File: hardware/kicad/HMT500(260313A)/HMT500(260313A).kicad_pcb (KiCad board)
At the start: 4 copper layers, 56.5 x 23 mm, 84 parts, among them J1 SM08B-GHS-TB, J2 TC2030-IDC-NL, J3 SM04B-SRSS-TB, J5 CHASSIS wire, U1 TPS26600PWPR, U10 TPS26611DDFR, U11 THVD2450DR, U12 OPA197IDBVR, U13 OPA197IDBVR, U14 SN74LVC2G32DCUR, U2 LMR36006BRNXR, U3 TPS7A2033PDBVR, U4 STM32G0B1CCT3, U5 PCAP04-AQFM-24, U6 ADS1220IPWR, U7 DAC8760IPWP, U8 DAC8760IPWP, U9 TPS26611DDFR

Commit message: Mech Rev H: outline equal to E+E EE364 per section, assembly procedure HMT500-A-001
- Exposed probe 12 x 34 (cap +5.5, 25 holes), G1/2 14, hex AF27 x 10, body dia 30,
  seal face to end cap 77, M12 15, overall 140
- Housing 30/25 with M26x1 R/LH turnbuckle, O-ring 24 x 1.5 in dia 27, end cap flange 4 mm AF27,
  M16x1.5 at x 71-77 (connector thread <= 6 mm); internals shifted -2, PCB placement unchanged
- place_pcb: plan coordinates relative to PCB front (DX), bores from params
- Assembly sim 23 checks NG 0; drawings, STEP, renders, JLCCNC package, docs, decision #30
- New assembly_procedure.py: 19-step procedure PDF with 3D step illustrations

Co-Authored-By: Claude Opus 5.5 <noreply@anthropic.com>
Claude-Session: https://claude.ai/code/session_01JA2o8uJsqp9Vzsg4b665ev
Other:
- board text added: "11.5-48.9 mm: width 23, bore 25 -> edge 3.6 / center 11.2 mm"
- board text removed: "11.5-48.9 mm: width 23, bore 27 -> edge 5.8 / center 12.2 mm"

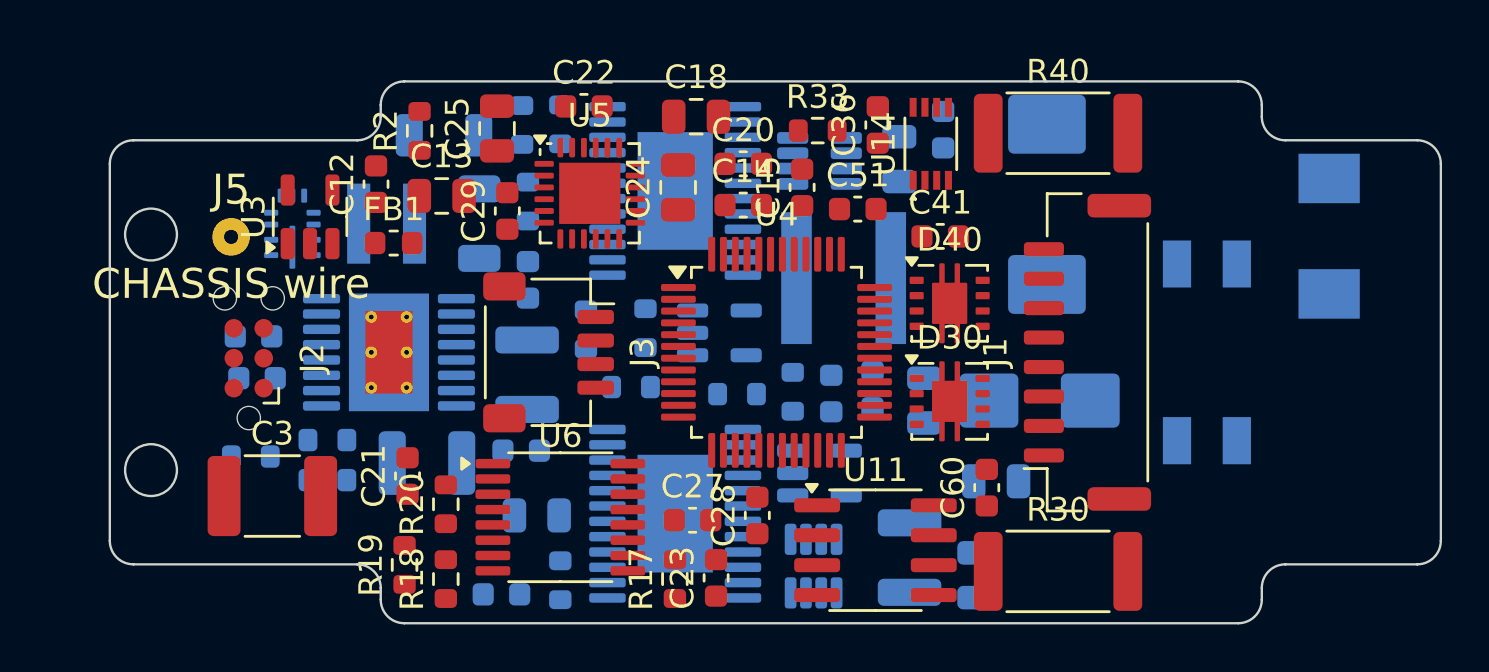
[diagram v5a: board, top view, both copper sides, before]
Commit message: Schematic v0.9 + placement rev 4: apply triple-review A/B items, re-review fixes
- Power: OVP 32.6 V (R5 36.5k), D2 TVS3301, C2 2.2u 100V, buck input 220n x2,
  U2 pin 3 = SW; TPS26611 +Vs emitter-follower clamp (Q1 MMBTA06, R50, D50 27V)
- RS-485: THVD2410, DE 10k pull-down (R60) for in-house bootloader
- MCU: SGOOD on PA0/PA4, CS_CDC PA15, VIN_SENSE PB0, LATCH/CS pull-ups,
  SWD no-connect removed, netlist checker flags no-connect on used pins
- Analog: OPA197 V+ = DAC AVDD, R31/R41 100k, local caps; X7R throughout
- New aux sheet; SOT-23 and R1206 footprints; parts list and JLC files
- Placement: pin-targeted hints, MCU decaps under U4, chassis parts grouped
  in front, J5 keep-out 3.3 mm, CHASSIS netclass; 102/102 parts placed
- Docs: final review H table, decision #32, circuit design, placement rev 4

Co-Authored-By: Claude Opus 5.5 <noreply@anthropic.com>
Claude-Session: https://claude.ai/code/session_01JA2o8uJsqp9Vzsg4b665ev
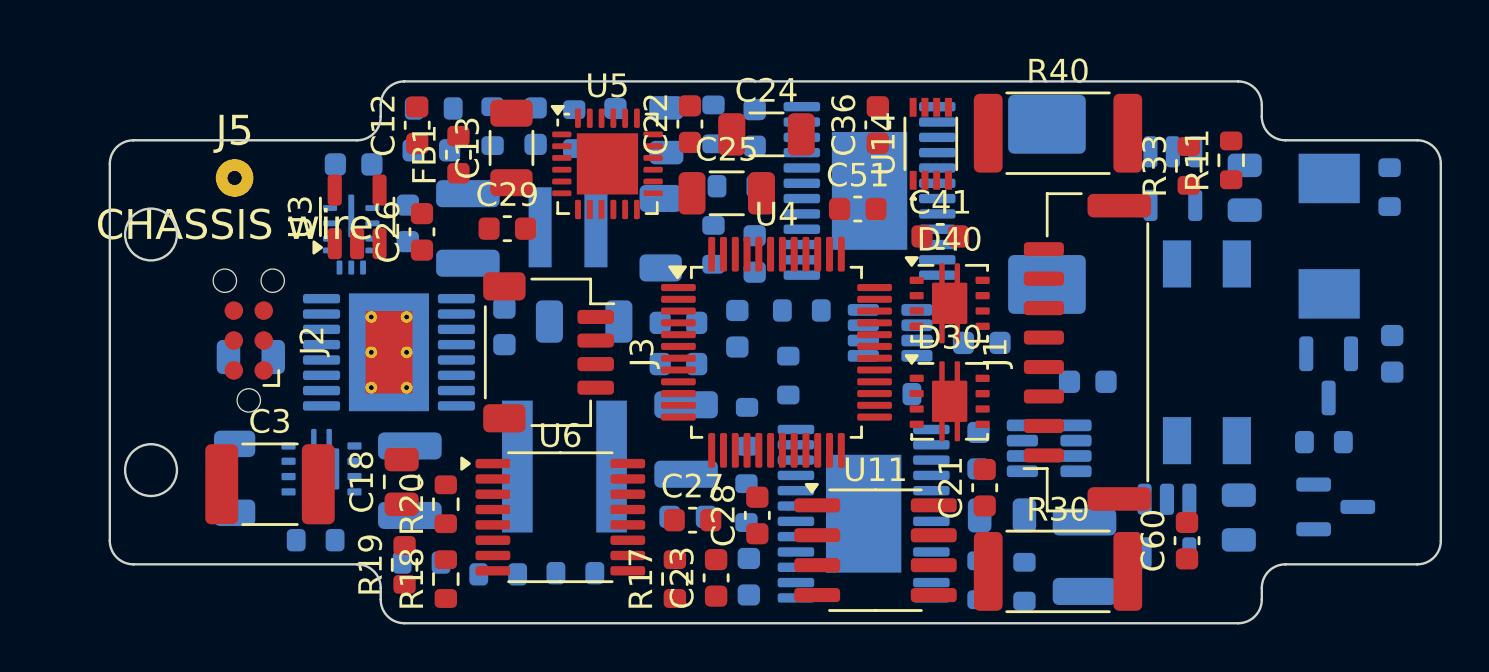
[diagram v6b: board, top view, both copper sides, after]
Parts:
- added C16: 220n 100V, Capacitor_SMD:C_0603_1608Metric, B.Cu at (110.3, 92.0)
- added C17: 220n 100V, Capacitor_SMD:C_0603_1608Metric, B.Cu at (112.7, 94.5)
- added C2: 2.2u 100V, Capacitor_SMD:C_1210_3225Metric, B.Cu at (112.7, 105.5)
- added C26: 1u, Capacitor_SMD:C_0603_1608Metric, F.Cu at (113.2, 94.9)
- added C30: 100n, Capacitor_SMD:C_0603_1608Metric, B.Cu at (124.5, 107.0)
- added C46: 100n, Capacitor_SMD:C_0603_1608Metric, B.Cu at (141.5, 101.2)
- added C53: 100n, Capacitor_SMD:C_0603_1608Metric, B.Cu at (154.4, 100.1)
- added C56: 100n, Capacitor_SMD:C_0603_1608Metric, B.Cu at (137.0, 99.6)
- added D50: BZX84C27, Package_TO_SOT_SMD:SOT-23, B.Cu at (152.0, 106.6)
- added Q1: MMBTA06, Package_TO_SOT_SMD:SOT-23, B.Cu at (151.7, 101.0)
- added R10: 10k, Resistor_SMD:R_0603_1608Metric, B.Cu at (126.6, 93.0)
- added R11: 10k, Resistor_SMD:R_0603_1608Metric, F.Cu at (147.6, 91.8)
- added R12: 100k, Resistor_SMD:R_0603_1608Metric, B.Cu at (119.8, 109.4)
- added R13: 100k, Resistor_SMD:R_0603_1608Metric, B.Cu at (125.6, 95.4)
- added R14: 100k 1%, Resistor_SMD:R_0603_1608Metric, B.Cu at (127.0, 103.2)
- added R15: 10k 1%, Resistor_SMD:R_0603_1608Metric, B.Cu at (128.8, 101.0)
- added R50: 10k, Resistor_SMD:R_0603_1608Metric, B.Cu at (151.5, 103.8)
- added R60: 10k, Resistor_SMD:R_0603_1608Metric, B.Cu at (127.0, 106.4)
- C13: footprint Capacitor_SMD:C_0805_2012Metric -> Capacitor_SMD:C_1206_3216Metric
- C14, C15, C20: moved to B.Cu
- C24: value 10u -> 22u 10V; footprint Capacitor_SMD:C_0805_2012Metric -> Capacitor_SMD:C_1206_3216Metric
- C25: value 4.7u -> 10u; footprint Capacitor_SMD:C_0805_2012Metric -> Capacitor_SMD:C_1206_3216Metric
- C27: value 10n -> 10n C0G
- D2: value SMBJ33CA -> TVS3301DRBR; footprint Diode_SMD:D_SMB -> HMT500_260313A:Texas_DRB0008A_PadFloat
- R2: value 1M -> 1M HV; footprint Resistor_SMD:R_0603_1608Metric -> Resistor_SMD:R_1206_3216Metric; moved to B.Cu
- R31, R41: value 10k -> 100k
- R5: value 41.2k 1% -> 36.5k 1%
- U11: value THVD2450DR -> THVD2410DR
- moved R41 32.2 mm to (154.3, 93.0)
- moved D2 30.6 mm to (109.0, 105.0)
- moved C1 28.6 mm to (106.0, 100.2), turned to 0 degrees
- moved C21 24.5 mm to (137.1, 105.8)
- moved C52 20.4 mm to (123.6, 90.6), turned to -90 degrees
- moved U13 20.3 mm to (145.1, 92.6), turned to -90 degrees
- moved C18 19.9 mm to (112.4, 105.5), turned to 90 degrees
- moved C42 19.8 mm to (137.9, 106.9)
- moved R34 17.8 mm to (136.9, 109.7)
- moved R2 16.7 mm to (105.3, 105.3), turned to -90 degrees
- moved R33 15.8 mm to (145.8, 92.1), turned to 90 degrees
- moved U12 14.9 mm to (144.9, 107.4), turned to -90 degrees
- moved C55 14.7 mm to (148.2, 93.0)
- moved C4 14.3 mm to (121.5, 90.4), turned to -90 degrees
- moved GDT1 14.3 mm to (119.3, 104.8)
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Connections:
- C45 pad 1: VIN_P -> DAC1_AVDD
- C55 pad 1: VIN_P -> DAC2_AVDD
- D2 pad 2: GND -> VIN_F
- U10 pad 6: VIN_P -> VS_CLAMP
- U12 pad 5: VIN_P -> DAC1_AVDD
- U13 pad 5: VIN_P -> DAC2_AVDD
- U2 pad 3: (no net) -> BUCK_SW
- U4 pad 11: (no net) -> OUT1_SGOOD
- U4 pad 15: (no net) -> OUT2_SGOOD
- U4 pad 19: CS_CDC -> VIN_SENSE
- U4 pad 30: OUT1_SGOOD -> (no net)
- U4 pad 31: OUT2_SGOOD -> (no net)
- U4 pad 37: (no net) -> CS_CDC
- U9 pad 6: VIN_P -> VS_CLAMP

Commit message: Map BOM to JLCPCB/LCSC parts (decision #34) and re-place
- 50 of 55 BOM lines have LCSC numbers (make_parts_list.LCSC); parts list
  gets LCSC / JLC class columns; JLC BOM and harness order filled
- Keep MCU (125 C grade), LMR36006, R19 precision ref and pulse resistors
  via JLC global sourcing
- LCSC-driven footprint changes: C6/C10 1210, C16/C17 0805, R1 2512,
  L2 XAL4040; C3 2 kV X7R 1812, GDT 2035-25, L1 SRF0905 (to verify)
- Re-placed: 102/102, netlist 77/77, assembly sim 23 OK

Co-Authored-By: Claude Opus 5.5 <noreply@anthropic.com>
Claude-Session: https://claude.ai/code/session_01JA2o8uJsqp9Vzsg4b665ev
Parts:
- C10, C6: footprint Capacitor_SMD:C_1206_3216Metric -> Capacitor_SMD:C_1210_3225Metric
- C16, C17: footprint Capacitor_SMD:C_0603_1608Metric -> Capacitor_SMD:C_0805_2012Metric
- C22: value 220p C0G 1% -> 330p C0G 1%
- C3: value 4.7n 2kV Y2 -> 4.7n 2kV
- L2: footprint Inductor_SMD:L_Coilcraft_XAL4030-XXX -> Inductor_SMD:L_Coilcraft_XAL4040-XXX
- R1: footprint Resistor_SMD:R_MELF_MMB-0207 -> Resistor_SMD:R_2512_6332Metric
- moved C11 13.7 mm to (123.5, 103.0)
- moved C4 13.1 mm to (125.2, 102.9)
- moved R8 9.49 mm to (116.8, 98.7), turned to -90 degrees
- moved C9 9.37 mm to (110.2, 92.2), turned to 0 degrees
- moved R15 9.26 mm to (138.1, 101.5), turned to 0 degrees
- moved C6 8.00 mm to (120.1, 90.7)
- moved R6 7.79 mm to (125.0, 96.3)
- moved R13 6.32 mm to (127.6, 101.4), turned to 0 degrees
- moved C10 5.35 mm to (120.1, 99.2), turned to 0 degrees
- moved C16 4.10 mm to (112.8, 95.3), turned to -90 degrees
- moved R14 3.75 mm to (130.1, 100.9)
- moved C30 3.25 mm to (124.5, 110.2)
- moved C7 3.25 mm to (124.5, 107.0)
- moved C17 2.46 mm to (113.7, 92.3), turned to 0 degrees
- moved L2 2.02 mm to (121.5, 94.9)
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
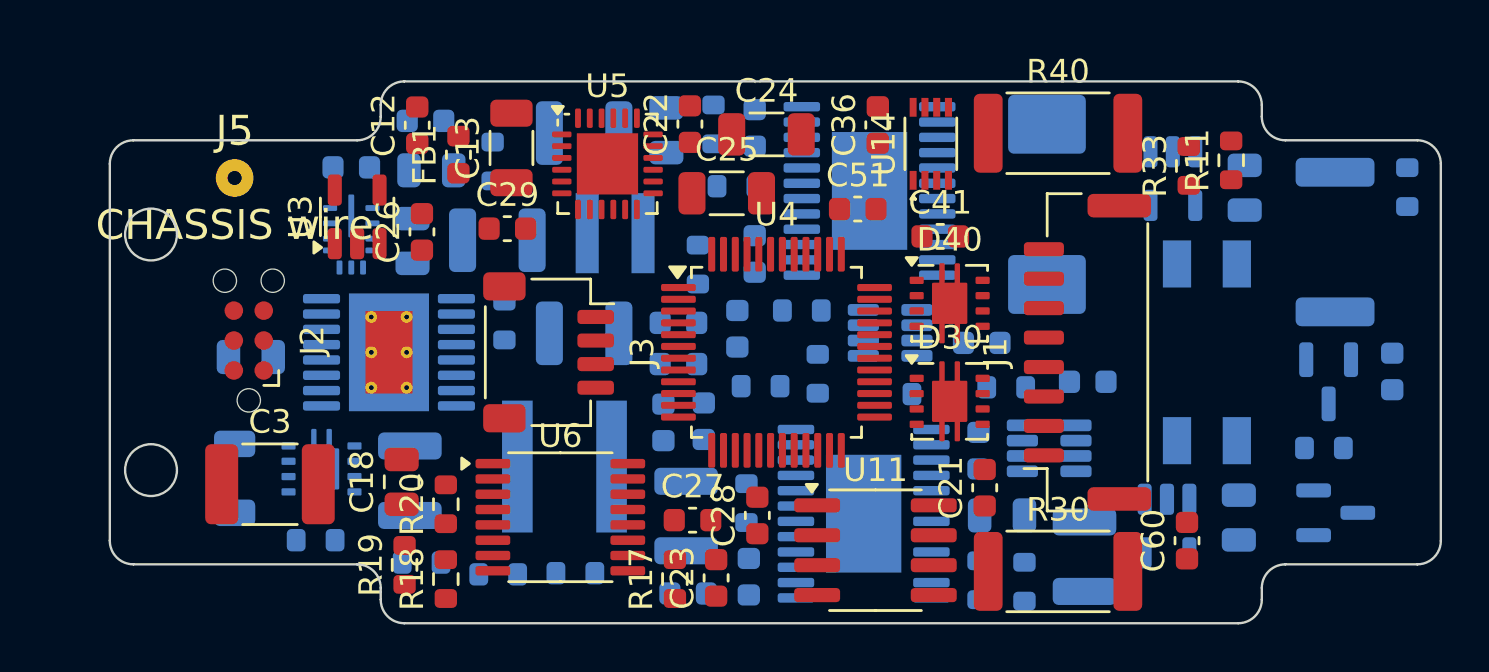
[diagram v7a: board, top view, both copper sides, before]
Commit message: Apply agreed external review items (decision #35)
- H01: series 100 V Schottky D3 (PMEG10010ELR) between D2 and eFuse IN
  (new net VIN_D) so negative surges no longer stress U1 IN-OUT
- H02: RS-485 bus TVS D60/D61 (TVS3301); U11 -> THVD2410DGKR (VSSOP-8)
- H04: +Vs clamp zener 27 V -> 24 V (BZX84C24LT1G)
- H08: ADS1220 IDAC fixed at 250 uA
- Room for new parts: C7 removed, 37 low-voltage R/C moved to 0402
  (LCSC basic where available); chassis parts keep CH_GAP between each other
- Placement 104/104, netlist 78/78, pcbnew DRC: no clearance errors,
  assembly sim 23 OK; parts list / JLC BOM updated
- docs/hw/external-review-response-260930.md: item responses, output load
  table, current budget, firmware requirements F1-F6, tests T1-T7

Co-Authored-By: Claude Opus 5.5 <noreply@anthropic.com>
Claude-Session: https://claude.ai/code/session_01JA2o8uJsqp9Vzsg4b665ev
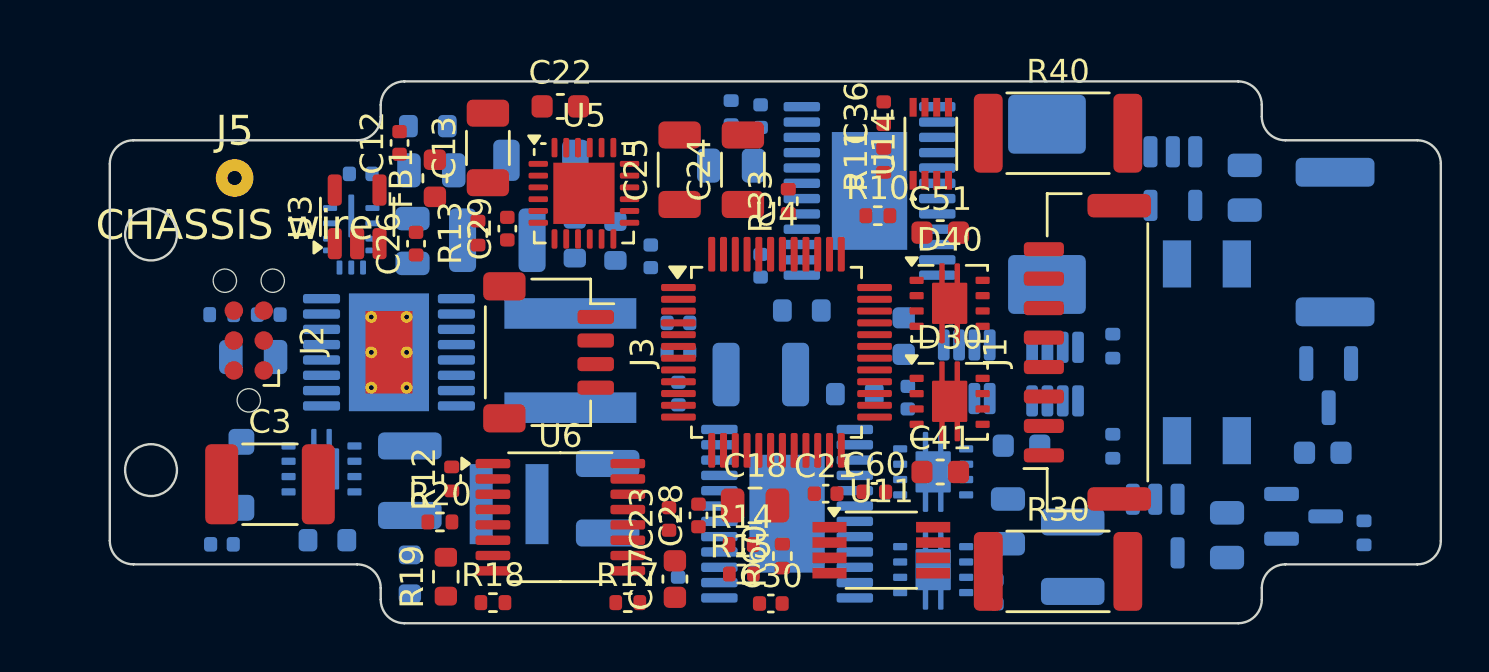
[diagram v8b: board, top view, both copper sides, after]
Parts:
- removed C7: 2.2u 100V, Capacitor_SMD:C_1210_3225Metric
- added D3: PMEG10010ELR, Diode_SMD:D_SOD-123F, B.Cu at (105.6, 105.2)
- added D60: TVS3301DRBR, HMT500_260313A:Texas_DRB0008A_PadFloat, B.Cu at (134.9, 109.2)
- added D61: TVS3301DRBR, HMT500_260313A:Texas_DRB0008A_PadFloat, B.Cu at (134.9, 105.1)
- C11, C12, C14, C15, C20, C21, C23, C26, C28, C29, C36, C4, C40, C44, C50, C54, C60, C8, C9: footprint Capacitor_SMD:C_0603_1608Metric -> Capacitor_SMD:C_0402_1005Metric
- C30: footprint Capacitor_SMD:C_0603_1608Metric -> Capacitor_SMD:C_0402_1005Metric; moved to F.Cu
- C46, C53, C56: value 100n -> 100n/50V
- D50: value BZX84C27 -> BZX84C24
- GDT1: value 2035-23-SM -> 2035-25-SM
- R10, R12, R13, R14, R15, R60: footprint Resistor_SMD:R_0603_1608Metric -> Resistor_SMD:R_0402_1005Metric; moved to F.Cu
- R11, R17, R18, R20, R31, R33, R34, R41, R44, R50, R8: footprint Resistor_SMD:R_0603_1608Metric -> Resistor_SMD:R_0402_1005Metric
- U11: value THVD2410DR -> THVD2410DGKR; footprint Package_SO:SOIC-8_3.9x4.9mm_P1.27mm -> Package_SO:VSSOP-8_3.0x3.0mm_P0.65mm
- moved C11 19.4 mm to (104.8, 108.2), turned to 0 degrees
- moved R2 18.7 mm to (118.3, 91.8), turned to 0 degrees
- moved R33 17.1 mm to (128.8, 93.6)
- moved C18 15.0 mm to (127.4, 106.5), turned to 0 degrees
- moved R11 14.8 mm to (132.8, 91.8)
- moved R5 14.6 mm to (119.7, 95.2), turned to -90 degrees
- moved R41 14.2 mm to (142.6, 99.7)
- moved R15 13.8 mm to (126.8, 109.4)
- moved R13 13.6 mm to (115.6, 94.9), turned to 90 degrees
- moved C60 13.4 mm to (132.4, 105.9), turned to 0 degrees
- moved C6 12.7 mm to (127.6, 100.9)
- moved L2 12.3 mm to (117.0, 106.4)
- moved R8 12.0 mm to (104.8, 98.4), turned to 0 degrees
- moved C41 10.0 mm to (135.2, 105.1)
- moved R14 7.95 mm to (126.8, 108.2), turned to 0 degrees
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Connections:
- C2 pad 1: VIN_F -> VIN_D
- R3 pad 1: VIN_F -> VIN_D
- U1 pad 1: VIN_F -> VIN_D
- U1 pad 2: VIN_F -> VIN_D
